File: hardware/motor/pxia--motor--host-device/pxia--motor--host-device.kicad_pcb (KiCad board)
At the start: 2 copper layers, 35.7 x 45.8 mm, 5 parts, among them J1 RJ45, U1 Teensy4.0, U2 max3490eesa+T

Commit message: finished schematics and most of pcb layout
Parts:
- added H1: M3, MountingHole:MountingHole_3.2mm_M3, F.Cu at (130.0, 60.2)
- added H2: M3, MountingHole:MountingHole_3.2mm_M3, F.Cu at (170.0, 60.0)
- added H3: M3, MountingHole:MountingHole_3.2mm_M3, F.Cu at (170.0, 130.0)
- added H4: M3, MountingHole:MountingHole_3.2mm_M3, F.Cu at (130.0, 130.0)
- added J2: Lolin D32 Pro 2.0.0 (ESP32) PIN01–16, Connector_PinSocket_2.54mm:PinSocket_1x16_P2.54mm_Vertical, F.Cu at (138.5, 82.0)
- added J3: GENERIC_UART, Connector_Molex:Molex_Nano-Fit_105313-xx04_1x04_P2.50mm_Horizontal, F.Cu at (153.8, 123.0)
- added J4: Lolin D32 Pro 2.0.0 (ESP32) PIN17–32, Connector_PinSocket_2.54mm:PinSocket_1x16_P2.54mm_Vertical, F.Cu at (161.5, 82.0)
- moved J1 73.8 mm to (154.3, 68.5), turned to 180 degrees
- moved R1 62.9 mm to (146.0, 75.9), turned to 90 degrees
- moved U1 62.8 mm to (150.0, 101.0), turned to 90 degrees
- moved U2 59.1 mm to (150.0, 77.5), turned to 90 degrees
- moved Re 58.1 mm to (154.0, 75.9), turned to -90 degrees
- renumbered R2 to Re
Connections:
- net /MCU_RX renamed /IO13
- net /MCU_TX renamed /IO14/T-CS
- J1 pad 3: GND -> unconnected-(J1-Pad3)
- J1 pad 4: GND -> unconnected-(J1-Pad3)
- J1 pad 5: GND -> unconnected-(J1-Pad3)
- J1 pad 6: GND -> unconnected-(J1-Pad3)
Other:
- board size 35.7 x 45.8 mm -> 50 x 80 mm
- board text added: "3V3"
- board text added: "GND"
- board text added: "RX"
- board text added: "TX"
- board text removed: "@TODO(FIND CORRECT FOOTPRINT ON JLCPCB)"

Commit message: updated PCBs
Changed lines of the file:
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@@
         (xy -3.683 0.508)
       ) (layer "F.SilkS") (width 0.1) (fill solid))
-    (pad "1" thru_hole circle locked (at -16.51 7.62 90) (size 1.6 1.6) (drill 1.1) (layers *.Cu *.Mask)
+    (pad "1" thru_hole rect locked (at -16.51 7.62 90) (size 1.6 1.6) (drill 1.1) (layers *.Cu *.Mask)
       (net 3 "GND") (pinfunction "GND") (pintype "power_in"))
     (pad "2" thru_hole circle locked (at -13.97 7.62 90) (size 1.6 1.6) (drill 1.1) (layers *.Cu *.Mask)
@@
     (pad "" np_thru_hole circle (at 7.18 0 270) (size 1.7 1.7) (drill 1.7) (layers *.Cu *.Mask))
     (pad "" np_thru_hole circle (at 7.18 7.5 270) (size 1.7 1.7) (drill 1.7) (layers *.Cu *.Mask))
-    (pad "1" thru_hole roundrect (at 0 0 270) (size 2.2 1.7) (drill 1.2) (layers *.Cu *.Mask) (roundrect_rratio 0.147059)
+    (pad "1" thru_hole oval (at 0 0 270) (size 2.2 1.7) (drill 1.2) (layers *.Cu *.Mask)
       (net 22 "+3V3") (pinfunction "Pin_1") (pintype "passive"))
     (pad "2" thru_hole oval (at 0 2.5 270) (size 2.2 1.7) (drill 1.2) (layers *.Cu *.Mask)
@@
     (pad "3" thru_hole oval (at 0 5 270) (size 2.2 1.7) (drill 1.2) (layers *.Cu *.Mask)
       (net 47 "/IO13") (pinfunction "Pin_3") (pintype "passive"))
-    (pad "4" thru_hole oval (at 0 7.5 270) (size 2.2 1.7) (drill 1.2) (layers *.Cu *.Mask)
+    (pad "4" thru_hole rect (at 0 7.5 270) (size 2.2 1.7) (drill 1.2) (layers *.Cu *.Mask)
       (net 3 "GND") (pinfunction "Pin_4") (pintype "passive"))
     (model "${KICAD6_3DMODEL_DIR}/Connector_Molex.3dshapes/Molex_Nano-Fit_105313-xx04_1x04_P2.50mm_Horizontal.wrl"
@@
     (fp_line (start 0.635 -1.27) (end 1.27 -0.635) (layer "F.Fab") (width 0.1))
     (fp_line (start 1.27 39.37) (end -1.27 39.37) (layer "F.Fab") (width 0.1))
-    (pad "1" thru_hole circle (at 0 0) (size 1.7 1.7) (drill 1) (layers *.Cu *.Mask)
+    (pad "1" thru_hole rect (at 0 0) (size 1.7 1.7) (drill 1) (layers *.Cu *.Mask)
       (net 3 "GND") (pinfunction "Pin_1") (pintype "passive"))
     (pad "2" thru_hole oval (at 0 2.54) (size 1.7 1.7) (drill 1) (layers *.Cu *.Mask)
@@
     )
   )
+  (gr_circle (center 148 82) (end 148.25 82) (layer "F.SilkS") (width 0.25) (fill none))
   (gr_line (start 173 55) (end 175 57) (layer "Edge.Cuts") (width 0.1))
   (gr_line (start 125 57) (end 125 133) (layer "Edge.Cuts") (width 0.1))
@@
     (effects (font (size 0.5 0.5) (thickness 0.1)))
   )
+  (gr_text "GND" (at 156.5 117.5) (layer "F.SilkS")
+    (effects (font (size 0.5 0.5) (thickness 0.1)) (justify right))
+  )
+  (gr_text "3V3" (at 143.5 112.5) (layer "F.SilkS")
+    (effects (font (size 0.5 0.5) (thickness 0.1)) (justify left))
+  )
+  (gr_text "TX" (at 136.5 107.5) (layer "F.SilkS")
+    (effects (font (size 0.5 0.5) (thickness 0.1)) (justify right))
+  )
+  (gr_text "GND" (at 163.5 82) (layer "F.SilkS")
+    (effects (font (size 0.5 0.5) (thickness 0.1)) (justify left))
+  )
+  (gr_text "RX" (at 156.5 99.5) (layer "F.SilkS")
+    (effects (font (size 0.5 0.5) (thickness 0.1)) (justify right))
+  )
   (gr_text "RX" (at 148.75 121) (layer "F.SilkS")
     (effects (font (size 0.5 0.5) (thickness 0.1)))
   )
+  (gr_text "TX" (at 156.5 94.5) (layer "F.SilkS")
+    (effects (font (size 0.5 0.5) (thickness 0.1)) (justify right))
+  )
+  (gr_text "3V3" (at 136.5 82) (layer "F.SilkS")
+    (effects (font (size 0.5 0.5) (thickness 0.1)) (justify right))
+  )
   (gr_text "3V3" (at 153.75 121) (layer "F.SilkS")
     (effects (font (size 0.5 0.5) (thickness 0.1)))
   )
+  (gr_text "RX" (at 136.5 112.5) (layer "F.SilkS")
+    (effects (font (size 0.5 0.5) (thickness 0.1)) (justify right))
+  )
   (gr_text "TX" (at 151.25 121) (layer "F.SilkS")

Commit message: finished routing
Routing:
- net /IO14/T-CS: track 0.00 -> 69.8 mm, vias 0 -> 2
- net /IO13: track 0.00 -> 66.9 mm, vias 0 -> 1
- net +3V3: track 0.00 -> 59.6 mm
- net /RX+: track 0.00 -> 16.4 mm
- net /TX-: track 0.00 -> 16.3 mm, vias 0 -> 3
- net /RX-: track 0.00 -> 14.1 mm
- net /TX+: track 0.00 -> 12.6 mm, vias 0 -> 2
- net unconnected-(J1-Pad3): track 0.00 -> 7.40 mm
- net GND: track 0.00 -> 1.11 mm, vias 0 -> 1
- added copper zone on F.Cu, net (none)
- added copper zone on B.Cu, net GND

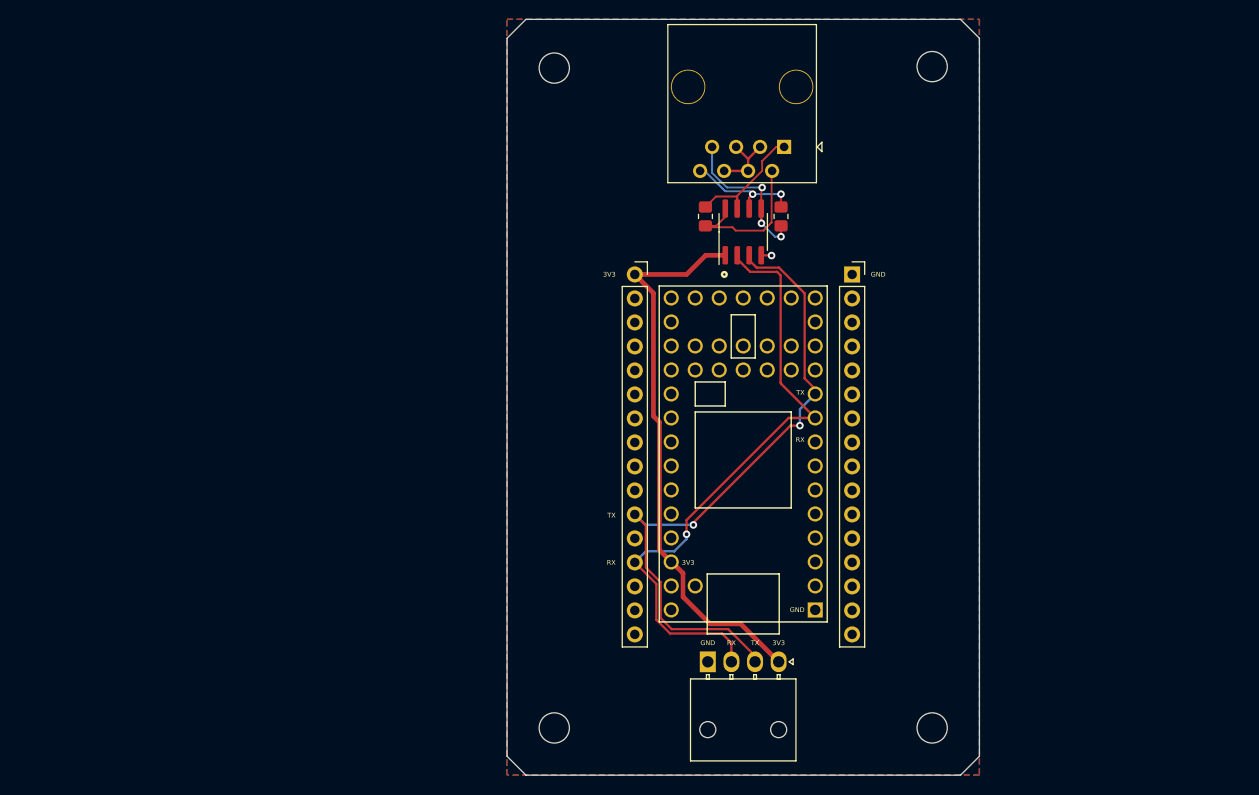
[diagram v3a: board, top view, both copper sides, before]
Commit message: added PicoW, finished PCB layout
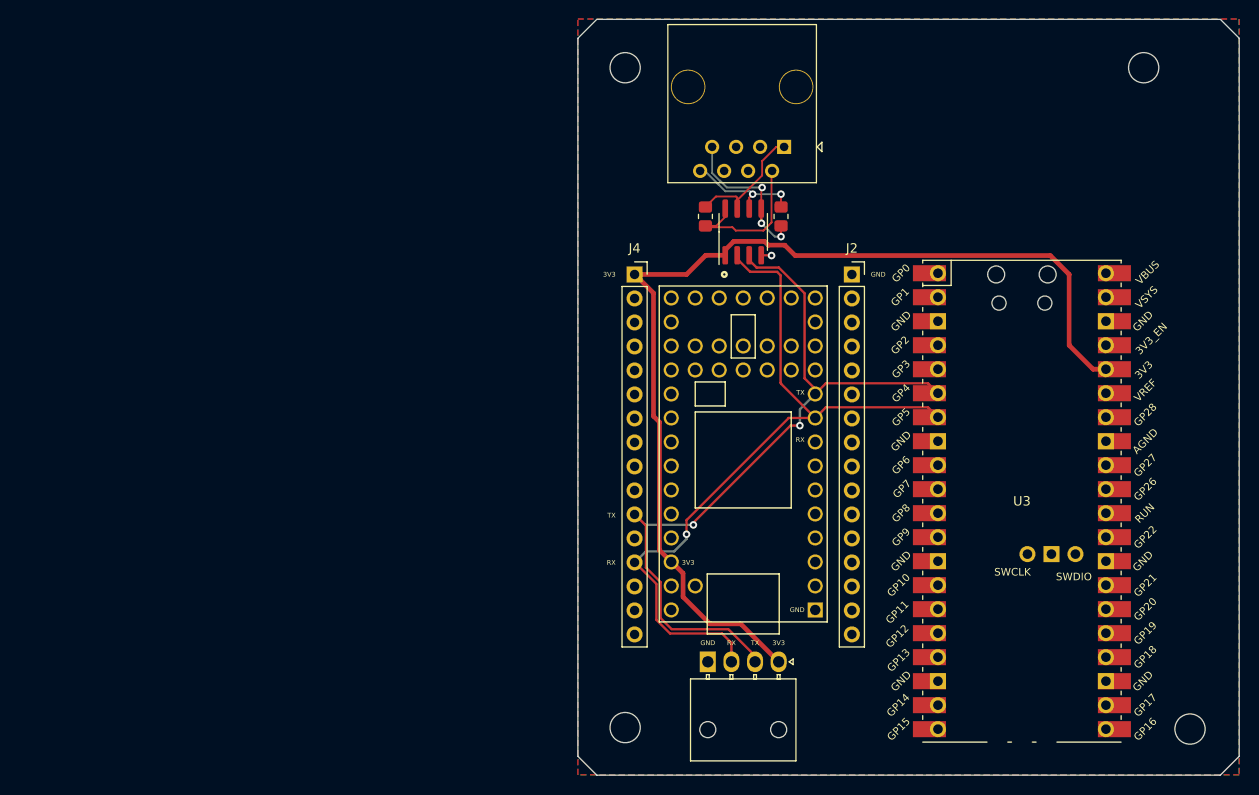
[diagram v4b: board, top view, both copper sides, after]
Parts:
- added U3: PicoW, PicoW:RPi_PicoW_SMD_TH, F.Cu at (179.5, 106.0)
- J2: value Lolin D32 Pro 2.0.0 (ESP32) PIN01–16 -> Lolin D32 Pro 2.0.0 (ESP32) PIN17–32
- J4: value Lolin D32 Pro 2.0.0 (ESP32) PIN17–32 -> Lolin D32 Pro 2.0.0 (ESP32) PIN01–16
- moved H3 27.3 mm to (197.3, 130.1)
- moved J4 23.0 mm to (138.5, 82.0)
- moved J2 23.0 mm to (161.5, 82.0)
- moved H2 22.4 mm to (192.4, 60.1)
- moved H1 7.50 mm to (137.5, 60.1)
- moved H4 7.50 mm to (137.5, 130.0)
- renumbered Re to R2
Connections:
- J1 pad 4: unconnected-(J1-Pad3) -> unconnected-(J1-Pad4)
- J1 pad 5: unconnected-(J1-Pad3) -> unconnected-(J1-Pad5)
- J1 pad 6: unconnected-(J1-Pad3) -> unconnected-(J1-Pad6)
- J2 pad 1: +3V3 -> GND
- J2 pad 10: /IO27/T-DC -> unconnected-(J2-Pad10)
- J2 pad 11: /IO14/T-CS -> unconnected-(J2-Pad11)
- J2 pad 12: /IO12/TS-CS -> unconnected-(J2-Pad12)
- J2 pad 13: /IO13 -> unconnected-(J2-Pad13)
- J2 pad 14: /EN -> unconnected-(J2-Pad14)
- J2 pad 15: /USB -> unconnected-(J2-Pad15)
- J2 pad 16: /BAT -> GND
- J2 pad 2: /RESET -> unconnected-(J2-Pad2)
- J2 pad 3: /VP -> unconnected-(J2-Pad3)
- J2 pad 4: /VN -> unconnected-(J2-Pad4)
- J2 pad 5: /IO34/A -> unconnected-(J2-Pad5)
- J2 pad 6: /IO32/A/T-LED -> unconnected-(J2-Pad6)
- J2 pad 7: /IO33/A/T-RST -> unconnected-(J2-Pad7)
- J2 pad 8: /IO25/DAC1 -> unconnected-(J2-Pad8)
- J2 pad 9: /IO26/DAC2 -> unconnected-(J2-Pad9)
- J3 pad 2: /IO14/T-CS -> /MCU_TX
- J3 pad 3: /IO13 -> /MCU_RX
- J4 pad 1: GND -> +3V3
- J4 pad 10: /NC -> unconnected-(J4-Pad10)
- J4 pad 11: /NC -> /MCU_TX
- J4 pad 12: /IO04/TF-CS -> unconnected-(J4-Pad12)
- J4 pad 13: /IO00 -> /MCU_RX
- J4 pad 14: /IO02 -> unconnected-(J4-Pad14)
- J4 pad 15: /IO15 -> unconnected-(J4-Pad15)
- J4 pad 16: GND -> unconnected-(J4-Pad16)
- J4 pad 2: /IO23/MOSI -> unconnected-(J4-Pad2)
- J4 pad 3: /IO22/SCL -> unconnected-(J4-Pad3)
- J4 pad 4: /TXD0 -> unconnected-(J4-Pad4)
- J4 pad 5: /RXD0 -> unconnected-(J4-Pad5)
- J4 pad 6: /IO21/SDA -> unconnected-(J4-Pad6)
- J4 pad 7: /IO19/MISO -> unconnected-(J4-Pad7)
- J4 pad 8: /IO18/SCK -> unconnected-(J4-Pad8)
- J4 pad 9: /IO05/SS -> unconnected-(J4-Pad9)
- U1 pad 10: /IO14/T-CS -> /MCU_TX
- U1 pad 9: /IO13 -> /MCU_RX
- U2 pad 2: /IO13 -> /MCU_RX
- U2 pad 3: /IO14/T-CS -> /MCU_TX
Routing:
- net /MCU_TX: track 0.00 -> 83.7 mm, vias 0 -> 2
- net /MCU_RX: track 0.00 -> 80.8 mm, vias 0 -> 1
- net /IO14/T-CS: track 69.8 -> 0.00 mm, vias 2 -> 0
- net /IO13: track 66.9 -> 0.00 mm, vias 1 -> 0
- net +3V3: track 59.6 -> 110.9 mm
- net unconnected-(J1-Pad3): track 7.40 -> 0.00 mm
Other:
- board size 50 x 80 mm -> 70 x 80 mm

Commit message: cleaned up, production ready
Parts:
- added J5: RJ45, Connector_RJ:RJ45_OST_PJ012-8P8CX_Vertical, F.Cu at (184.0, 68.5)
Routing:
- net /RX-: track 14.1 -> 56.3 mm, vias 0 -> 2
- net /RX+: track 16.4 -> 57.4 mm, vias 0 -> 2
- net /TX-: track 16.3 -> 43.8 mm
- net /TX+: track 12.6 -> 36.4 mm

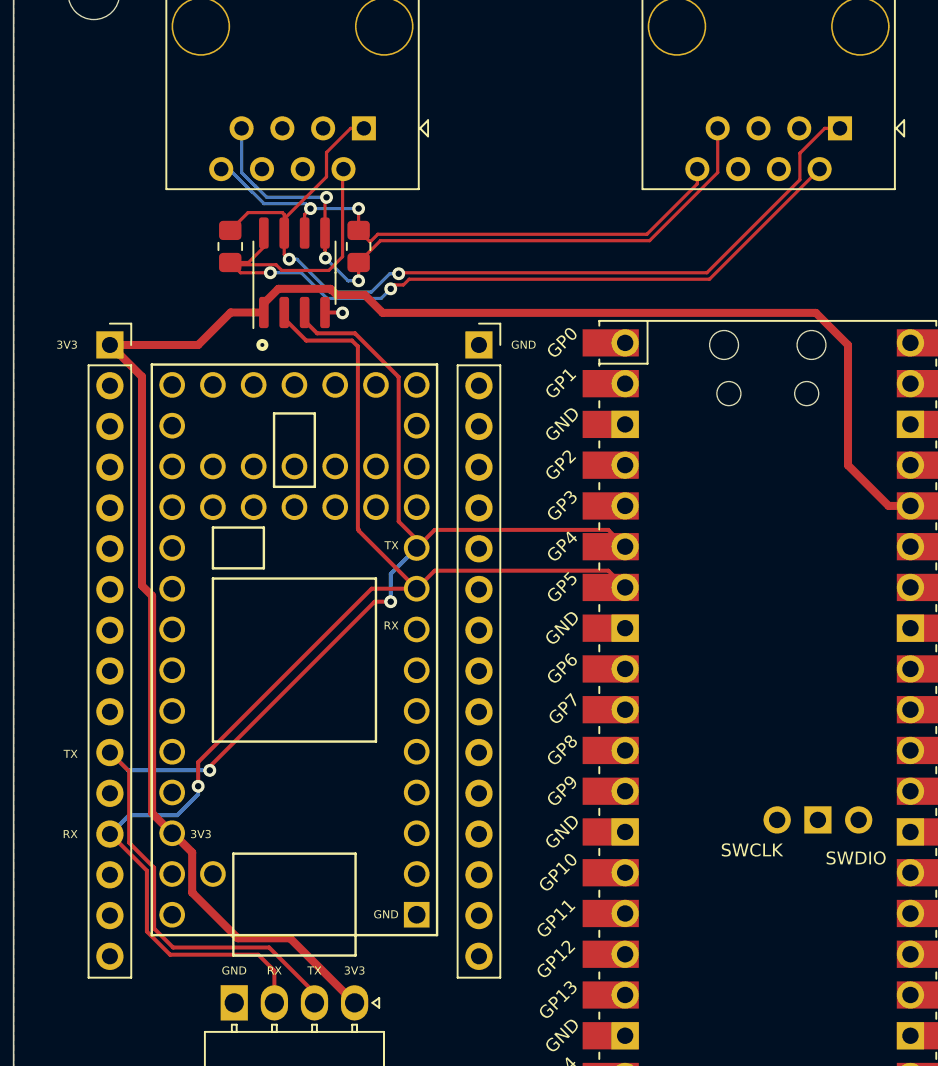
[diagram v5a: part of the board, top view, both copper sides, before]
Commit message: updated documentation, fixed wrong wiring
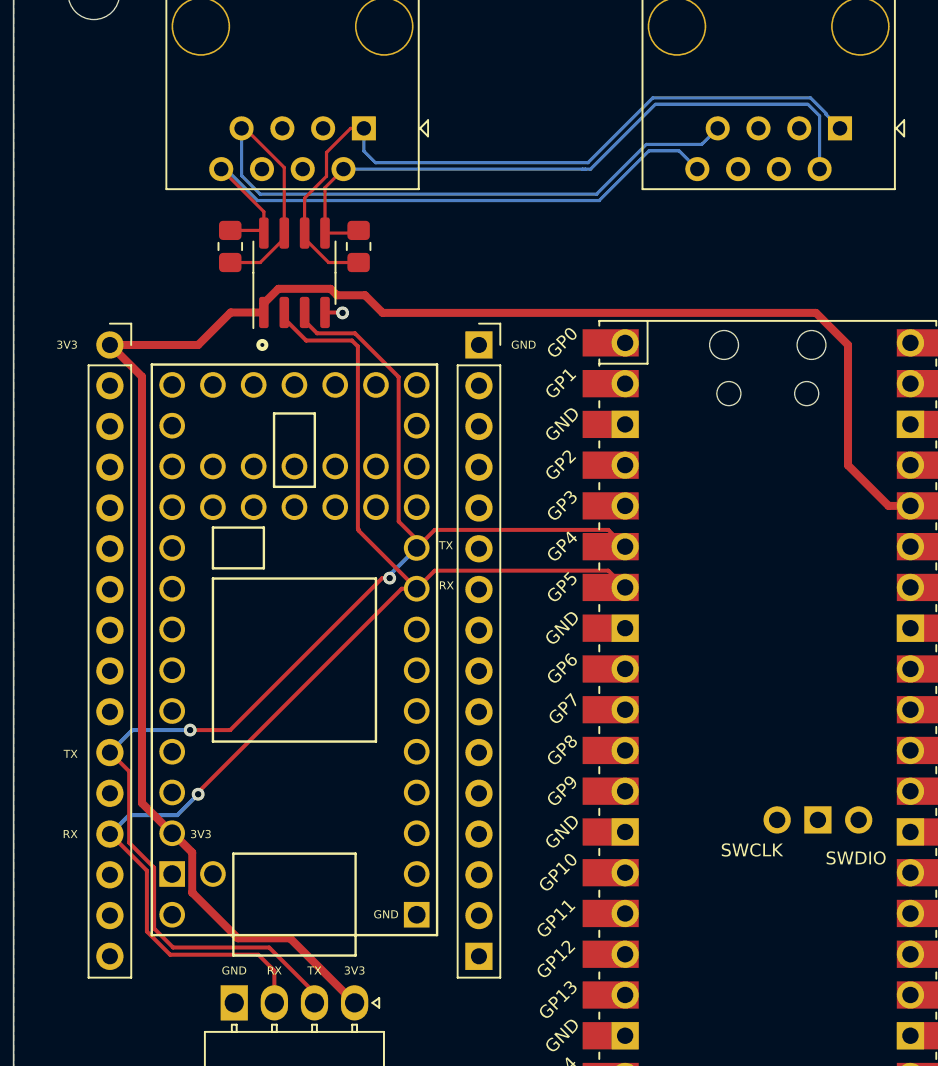
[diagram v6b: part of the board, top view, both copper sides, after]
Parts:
- moved R1 8.00 mm to (154.0, 75.9), turned to -90 degrees
- moved R2 8.00 mm to (146.0, 75.9)
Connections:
- U2 pad 5: /TX- -> /RX+
- U2 pad 6: /TX+ -> /RX-
- U2 pad 7: /RX- -> /TX-
- U2 pad 8: /RX+ -> /TX+
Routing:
- net /RX+: track 57.4 -> 41.6 mm, vias 2 -> 0
- net /RX-: track 56.3 -> 46.7 mm, vias 2 -> 0
- net /TX-: track 43.8 -> 46.9 mm, vias 3 -> 0
- net /TX+: track 36.4 -> 39.5 mm, vias 2 -> 0
- net /MCU_TX: track 83.7 -> 81.7 mm
- net /MCU_RX: track 80.8 -> 79.7 mm
